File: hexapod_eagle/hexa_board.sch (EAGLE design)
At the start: 68 parts, among them X1 ARK2, X2 ARK1

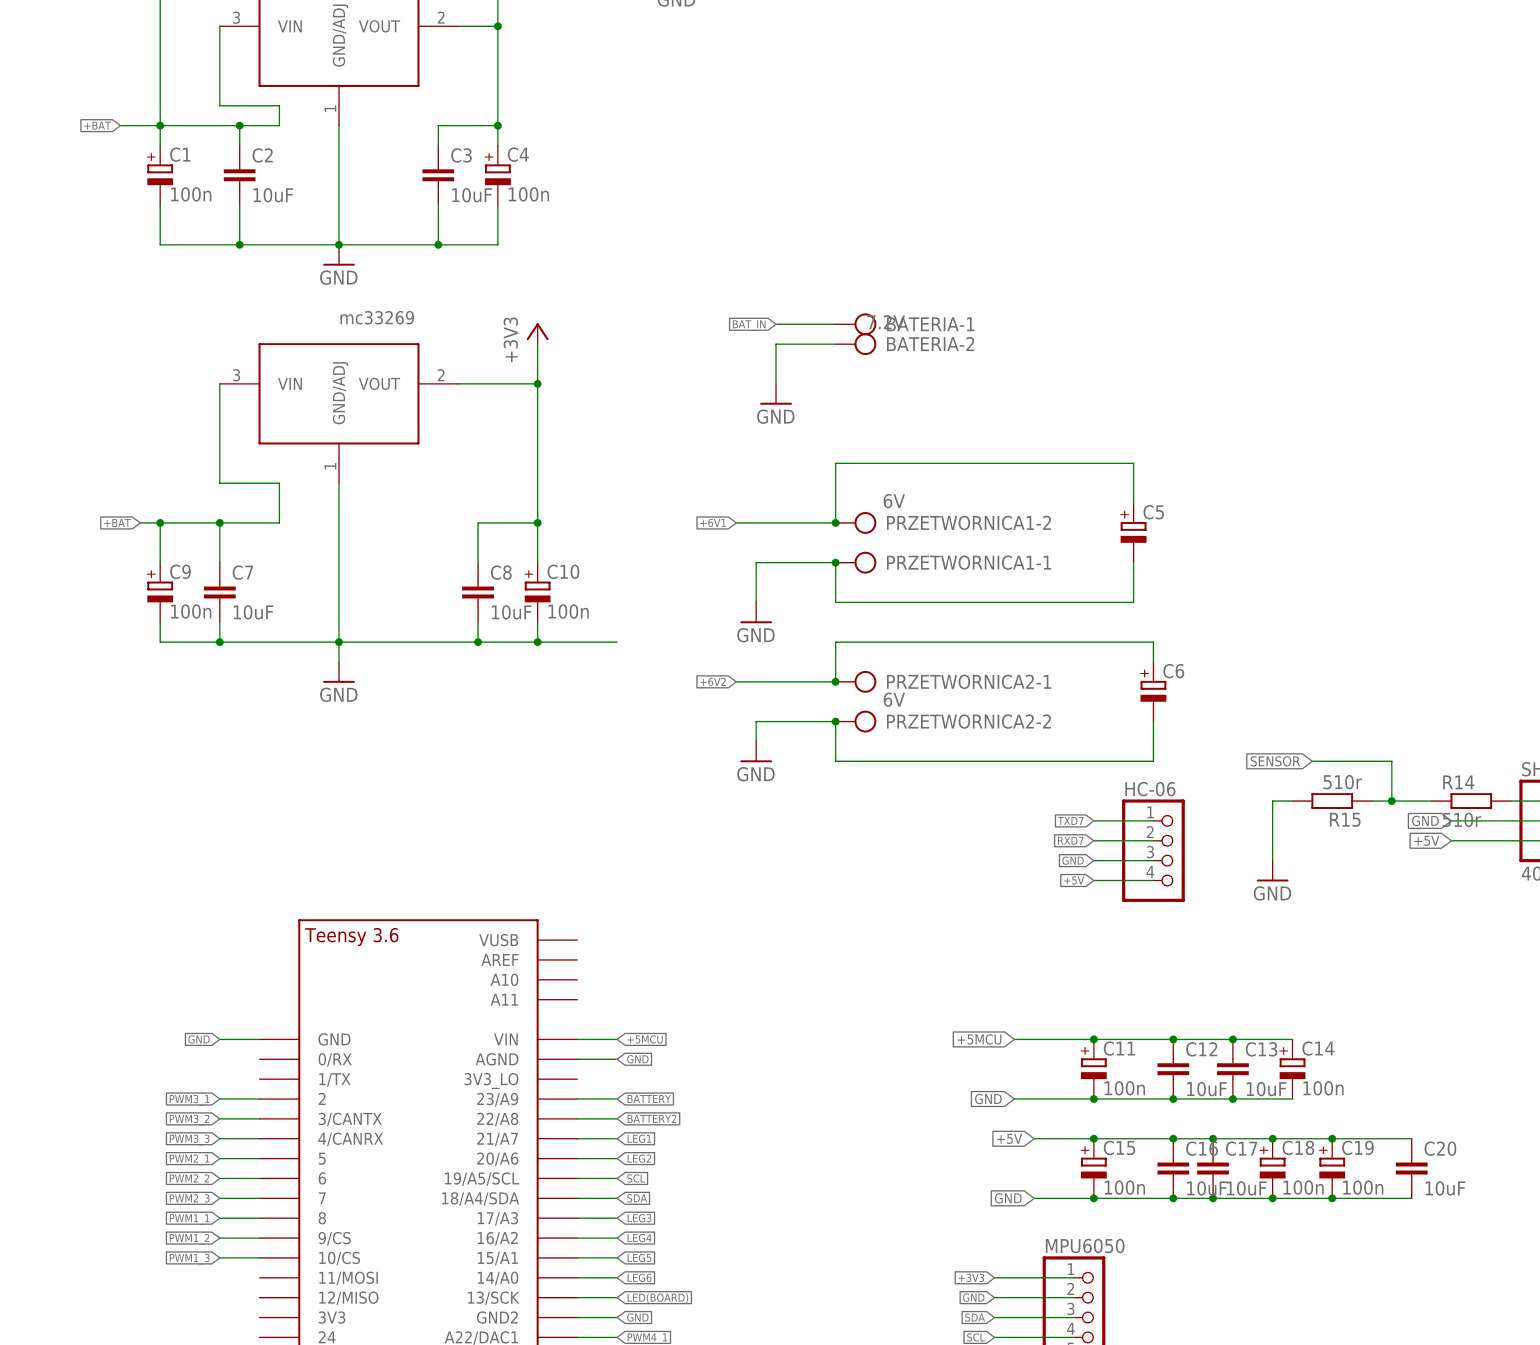
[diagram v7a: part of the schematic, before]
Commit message: Update eagle files
Change some capacitors package.
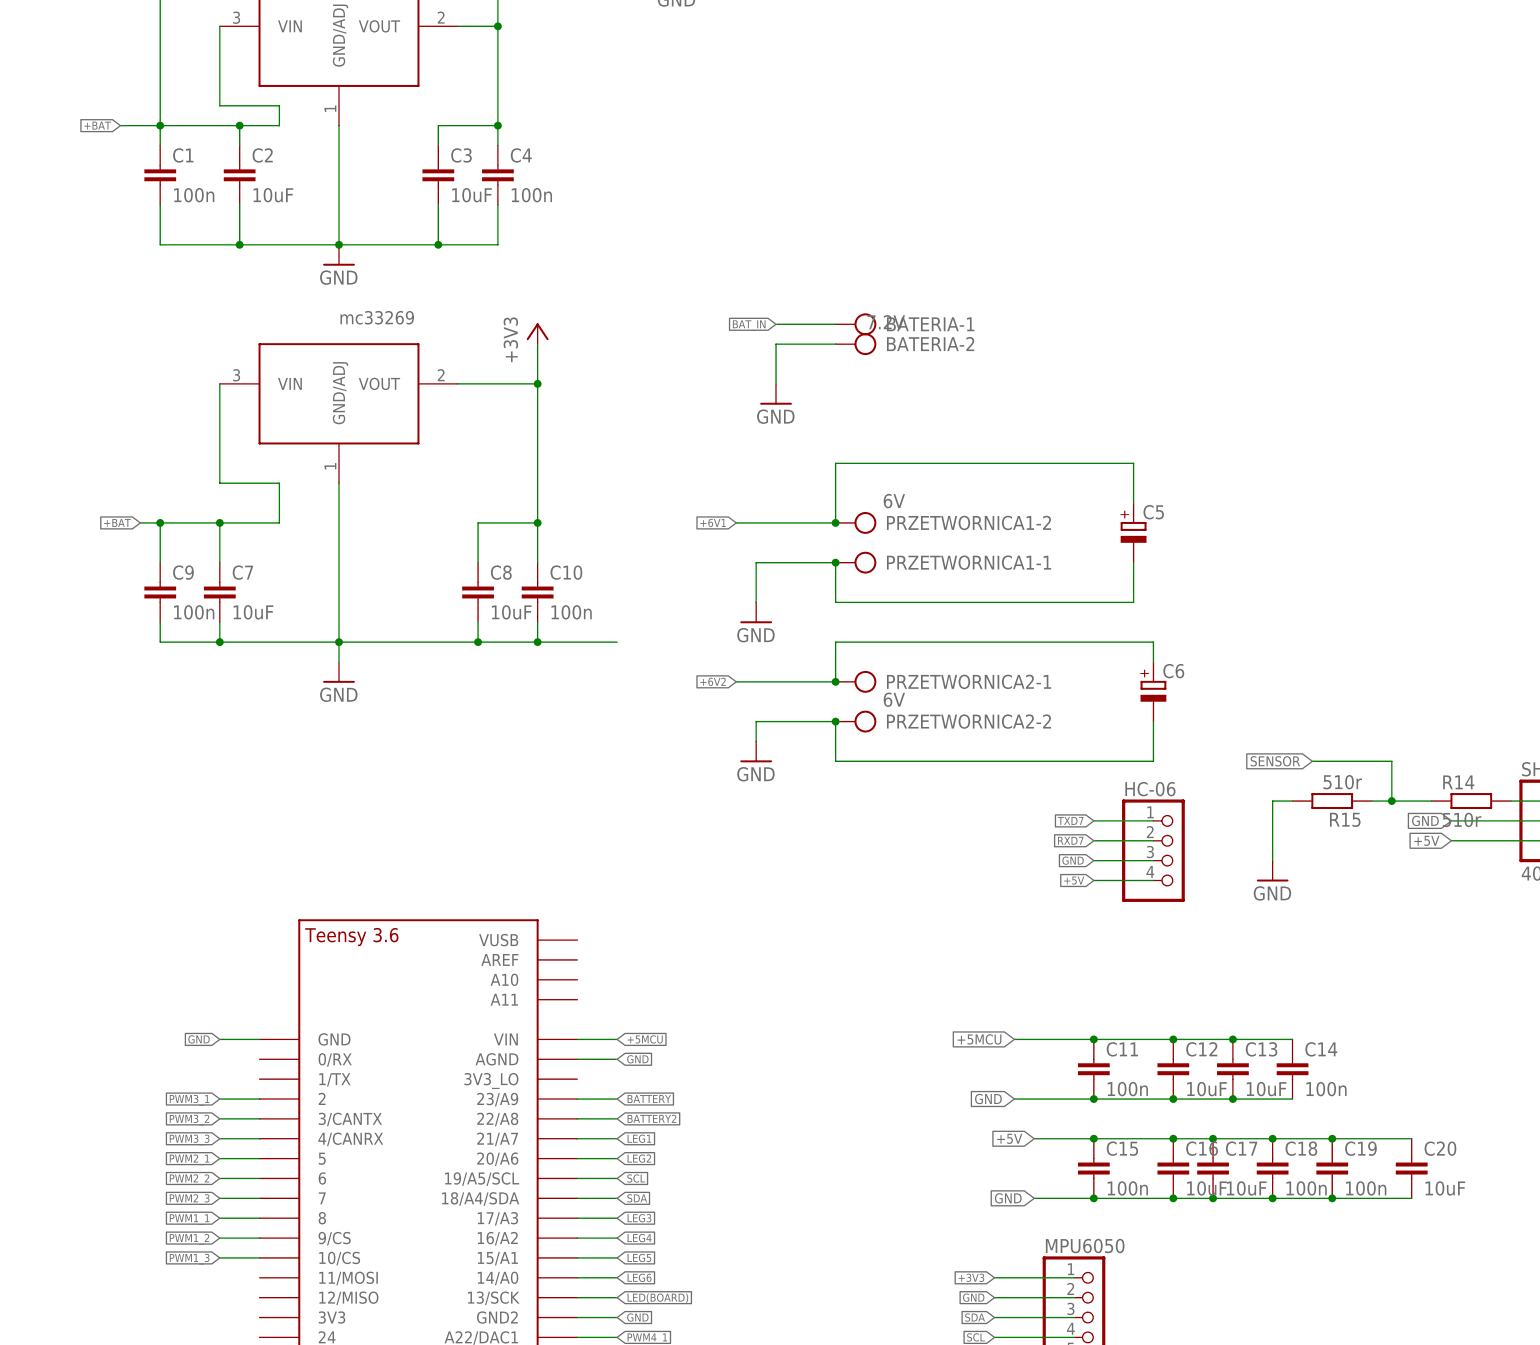
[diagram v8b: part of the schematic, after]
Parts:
- C1, C10, C11, C14, C15, C18, C19, C4, C9: device rcl:CPOL-EUSMCA -> rcl:C-EUC0805
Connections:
- net +3V3: now also C10.1; no longer C10.+
- net +5MCU: now also C11.1, C14.1; no longer C11.+, C14.+
- net +5V: now also C15.1, C18.1, C19.1, C4.1; no longer C15.+, C18.+, C19.+, C4.+
- net +BAT: now also C1.1, C9.1; no longer C1.+, C9.+
- net GND: now also C1.2, C10.2, C11.2, C14.2, C15.2, C18.2, C19.2, C4.2, C9.2; no longer C1.-, C10.-, C11.-, C14.-, C15.-, C18.-, C19.-, C4.-, C9.-
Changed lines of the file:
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@@
 <part name="GND12" library="supply1" deviceset="GND" device=""/>
 <part name="GND13" library="supply1" deviceset="GND" device=""/>
-<part name="C9" library="rcl" deviceset="CPOL-EU" device="SMCA" value="100n"/>
-<part name="C10" library="rcl" deviceset="CPOL-EU" device="SMCA" value="100n"/>
+<part name="C9" library="rcl" deviceset="C-EU" device="C0805" value="100n"/>
+<part name="C10" library="rcl" deviceset="C-EU" device="C0805" value="100n"/>
 <part name="TEENSY41" library="teensy" deviceset="TEENSY_3.5/3.6_BASIC" device=""/>
 <part name="GND1" library="supply1" deviceset="GND" device=""/>
-<part name="C1" library="rcl" deviceset="CPOL-EU" device="SMCA" value="100n"/>
+<part name="C1" library="rcl" deviceset="C-EU" device="C0805" value="100n"/>
 <part name="C2" library="rcl" deviceset="C-EU" device="C1206" value="10uF"/>
 <part name="C3" library="rcl" deviceset="C-EU" device="C1206" value="10uF"/>
-<part name="C4" library="rcl" deviceset="CPOL-EU" device="SMCA" value="100n"/>
+<part name="C4" library="rcl" deviceset="C-EU" device="C0805" value="100n"/>
 <part name="P+1" library="supply1" deviceset="+5V" device=""/>
 <part name="GND3" library="supply1" deviceset="GND" device=""/>
@@
 <part name="C6" library="rcl" deviceset="CPOL-EU" device="150CLZ-1014"/>
 <part name="WLACZNIK1" library="switch" deviceset="255SB" device="" value="7.2V"/>
-<part name="C11" library="rcl" deviceset="CPOL-EU" device="SMCA" value="100n"/>
+<part name="C11" library="rcl" deviceset="C-EU" device="C0805" value="100n"/>
 <part name="C12" library="rcl" deviceset="C-EU" device="C1206" value="10uF"/>
 <part name="C13" library="rcl" deviceset="C-EU" device="C1206" value="10uF"/>
-<part name="C14" library="rcl" deviceset="CPOL-EU" device="SMCA" value="100n"/>
-<part name="C15" library="rcl" deviceset="CPOL-EU" device="SMCA" value="100n"/>
+<part name="C14" library="rcl" deviceset="C-EU" device="C0805" value="100n"/>
+<part name="C15" library="rcl" deviceset="C-EU" device="C0805" value="100n"/>
 <part name="C16" library="rcl" deviceset="C-EU" device="C1206" value="10uF"/>
 <part name="R14" library="rcl" deviceset="R-EU_" device="R0805" value="510r"/>
@@
 <part name="GND2" library="supply1" deviceset="GND" device=""/>
 <part name="C17" library="rcl" deviceset="C-EU" device="C1206" value="10uF"/>
-<part name="C18" library="rcl" deviceset="CPOL-EU" device="SMCA" value="100n"/>
-<part name="C19" library="rcl" deviceset="CPOL-EU" device="SMCA" value="100n"/>
+<part name="C18" library="rcl" deviceset="C-EU" device="C0805" value="100n"/>
+<part name="C19" library="rcl" deviceset="C-EU" device="C0805" value="100n"/>
 <part name="C20" library="rcl" deviceset="C-EU" device="C1206" value="10uF"/>
 </parts>
@@
 <pinref part="+3V5" gate="G$1" pin="+3V3"/>
 <wire x1="50.8" y1="218.44" x2="50.8" y2="236.22" width="0.1524" layer="91"/>
-<pinref part="C10" gate="G$1" pin="+"/>
+<pinref part="C10" gate="G$1" pin="1"/>
 <wire x1="50.8" y1="236.22" x2="50.8" y2="241.3" width="0.1524" layer="91"/>
 <wire x1="50.8" y1="218.44" x2="50.8" y2="213.36" width="0.1524" layer="91"/>
@@
 <pinref part="GND11" gate="1" pin="GND"/>
 <wire x1="25.4" y1="200.66" x2="25.4" y2="203.2" width="0.1524" layer="91"/>
-<pinref part="C9" gate="G$1" pin="-"/>
+<pinref part="C9" gate="G$1" pin="2"/>
 <wire x1="10.16" y1="203.2" x2="2.54" y2="203.2" width="0.1524" layer="91"/>
 <wire x1="2.54" y1="203.2" x2="2.54" y2="205.74" width="0.1524" layer="91"/>
 <junction x="10.16" y="203.2"/>
-<pinref part="C10" gate="G$1" pin="-"/>
+<pinref part="C10" gate="G$1" pin="2"/>
 <wire x1="43.18" y1="203.2" x2="50.8" y2="203.2" width="0.1524" layer="91"/>
 <wire x1="50.8" y1="203.2" x2="50.8" y2="205.74" width="0.1524" layer="91"/>
@@
 <segment>
 <pinref part="GND1" gate="1" pin="GND"/>
-<pinref part="C1" gate="G$1" pin="-"/>
+<pinref part="C1" gate="G$1" pin="2"/>
 <wire x1="25.4" y1="254" x2="12.7" y2="254" width="0.1524" layer="91"/>
 <wire x1="12.7" y1="254" x2="2.54" y2="254" width="0.1524" layer="91"/>
@@
 <wire x1="25.4" y1="254" x2="38.1" y2="254" width="0.1524" layer="91"/>
 <wire x1="38.1" y1="254" x2="38.1" y2="259.08" width="0.1524" layer="91"/>
-<pinref part="C4" gate="G$1" pin="-"/>
+<pinref part="C4" gate="G$1" pin="2"/>
 <wire x1="38.1" y1="254" x2="45.72" y2="254" width="0.1524" layer="91"/>
 <wire x1="45.72" y1="254" x2="45.72" y2="259.08" width="0.1524" layer="91"/>
@@
 <segment>
 <pinref part="C12" gate="G$1" pin="2"/>
-<pinref part="C11" gate="G$1" pin="-"/>
+<pinref part="C11" gate="G$1" pin="2"/>
 <wire x1="132.08" y1="144.78" x2="121.92" y2="144.78" width="0.1524" layer="91"/>
 <wire x1="121.92" y1="144.78" x2="111.76" y2="144.78" width="0.1524" layer="91"/>
@@
 <wire x1="139.7" y1="144.78" x2="132.08" y2="144.78" width="0.1524" layer="91"/>
 <junction x="132.08" y="144.78"/>
-<pinref part="C14" gate="G$1" pin="-"/>
+<pinref part="C14" gate="G$1" pin="2"/>
 <wire x1="139.7" y1="144.78" x2="147.32" y2="144.78" width="0.1524" layer="91"/>
 <junction x="139.7" y="144.78"/>
 </segment>
 <segment>
-<pinref part="C15" gate="G$1" pin="-"/>
+<pinref part="C15" gate="G$1" pin="2"/>
 <pinref part="C16" gate="G$1" pin="2"/>
 <wire x1="121.92" y1="132.08" x2="132.08" y2="132.08" width="0.1524" layer="91"/>
@@
 <wire x1="132.08" y1="132.08" x2="137.16" y2="132.08" width="0.1524" layer="91"/>
 <junction x="132.08" y="132.08"/>
-<pinref part="C18" gate="G$1" pin="-"/>
+<pinref part="C18" gate="G$1" pin="2"/>
 <wire x1="137.16" y1="132.08" x2="144.78" y2="132.08" width="0.1524" layer="91"/>
 <junction x="137.16" y="132.08"/>
-<pinref part="C19" gate="G$1" pin="-"/>
+<pinref part="C19" gate="G$1" pin="2"/>
 <wire x1="144.78" y1="132.08" x2="152.4" y2="132.08" width="0.1524" layer="91"/>
 <junction x="144.78" y="132.08"/>
@@
 <wire x1="17.78" y1="269.24" x2="12.7" y2="269.24" width="0.1524" layer="91"/>
 <wire x1="12.7" y1="269.24" x2="12.7" y2="266.7" width="0.1524" layer="91"/>
-<pinref part="C1" gate="G$1" pin="+"/>
+<pinref part="C1" gate="G$1" pin="1"/>
 <wire x1="12.7" y1="269.24" x2="2.54" y2="269.24" width="0.1524" layer="91"/>
 <wire x1="2.54" y1="269.24" x2="2.54" y2="266.7" width="0.1524" layer="91"/>
@@
 <junction x="10.16" y="218.44"/>
 <label x="0" y="218.44" size="1.016" layer="95" rot="R180" xref="yes"/>
-<pinref part="C9" gate="G$1" pin="+"/>
+<pinref part="C9" gate="G$1" pin="1"/>
 <wire x1="2.54" y1="218.44" x2="0" y2="218.44" width="0.1524" layer="91"/>
 <wire x1="2.54" y1="213.36" x2="2.54" y2="218.44" width="0.1524" layer="91"/>
@@
 <pinref part="C3" gate="G$1" pin="1"/>
 <wire x1="38.1" y1="269.24" x2="38.1" y2="266.7" width="0.1524" layer="91"/>
-<pinref part="C4" gate="G$1" pin="+"/>
+<pinref part="C4" gate="G$1" pin="1"/>
 <wire x1="38.1" y1="269.24" x2="45.72" y2="269.24" width="0.1524" layer="91"/>
 <wire x1="45.72" y1="269.24" x2="45.72" y2="266.7" width="0.1524" layer="91"/>
@@
 </segment>
 <segment>
-<pinref part="C15" gate="G$1" pin="+"/>
+<pinref part="C15" gate="G$1" pin="1"/>
 <pinref part="C16" gate="G$1" pin="1"/>
 <wire x1="121.92" y1="139.7" x2="132.08" y2="139.7" width="0.1524" layer="91"/>
@@
 <wire x1="132.08" y1="139.7" x2="137.16" y2="139.7" width="0.1524" layer="91"/>
 <junction x="132.08" y="139.7"/>
-<pinref part="C18" gate="G$1" pin="+"/>
+<pinref part="C18" gate="G$1" pin="1"/>
 <wire x1="137.16" y1="139.7" x2="144.78" y2="139.7" width="0.1524" layer="91"/>
 <junction x="137.16" y="139.7"/>
-<pinref part="C19" gate="G$1" pin="+"/>
+<pinref part="C19" gate="G$1" pin="1"/>
 <wire x1="144.78" y1="139.7" x2="152.4" y2="139.7" width="0.1524" layer="91"/>
 <junction x="144.78" y="139.7"/>
@@
 <segment>
 <pinref part="C12" gate="G$1" pin="1"/>
-<pinref part="C11" gate="G$1" pin="+"/>
+<pinref part="C11" gate="G$1" pin="1"/>
 <wire x1="132.08" y1="152.4" x2="121.92" y2="152.4" width="0.1524" layer="91"/>
 <wire x1="121.92" y1="152.4" x2="111.76" y2="152.4" width="0.1524" layer="91"/>
@@
 <wire x1="132.08" y1="152.4" x2="139.7" y2="152.4" width="0.1524" layer="91"/>
 <junction x="132.08" y="152.4"/>
-<pinref part="C14" gate="G$1" pin="+"/>
+<pinref part="C14" gate="G$1" pin="1"/>
 <wire x1="139.7" y1="152.4" x2="147.32" y2="152.4" width="0.1524" layer="91"/>
 <junction x="139.7" y="152.4"/>
